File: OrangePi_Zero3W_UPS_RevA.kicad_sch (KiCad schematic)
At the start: 33 parts, among them J1 ORANGE_PI_ZERO_3W_HEADER, J2 BATTERY_1S_PROTECTED_NTC, J3 USB_C_POWER_INPUT, Q1 STL9P3LLH6, SW1 POWER / QON, U1 MAX17048G_T10, U2 BQ25895RTWR, U3 STUSB4500LQTR

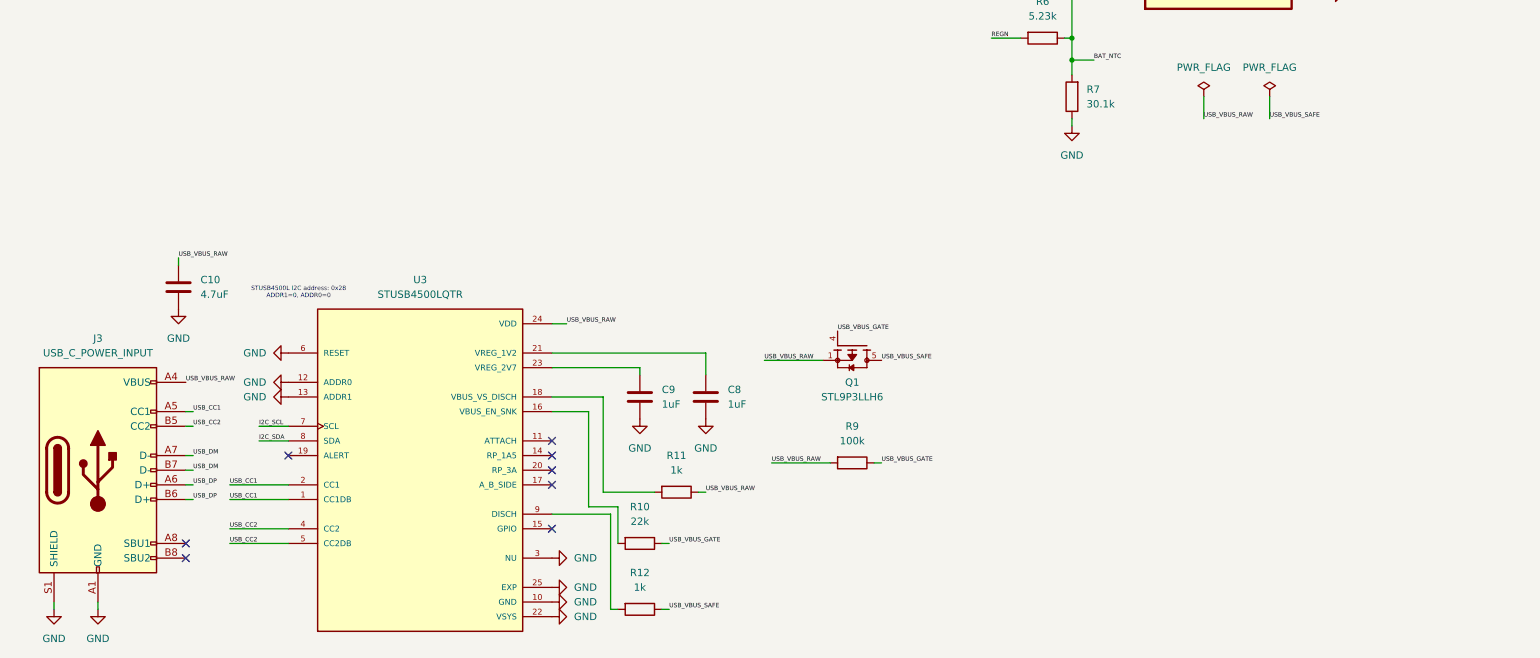
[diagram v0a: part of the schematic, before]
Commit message: Phase 5B.2D: add USB-C ESD and VBUS surge protection
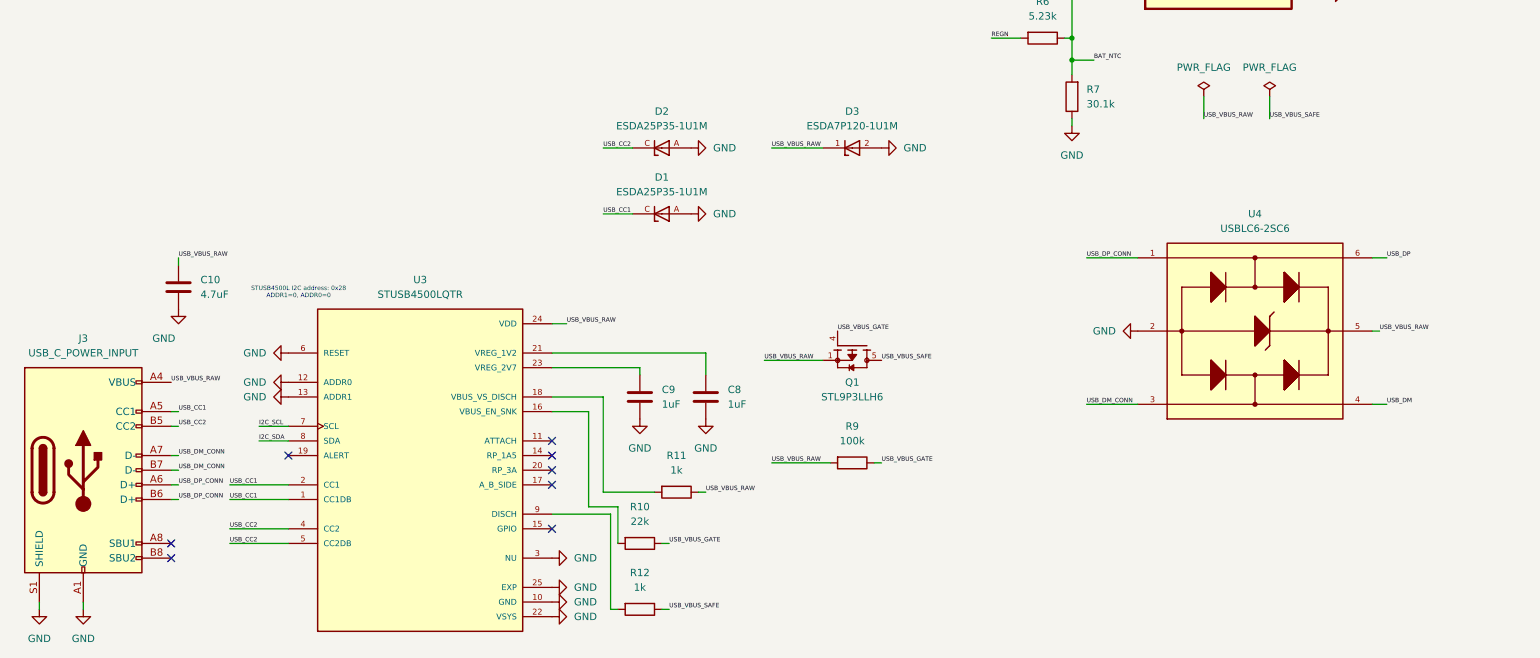
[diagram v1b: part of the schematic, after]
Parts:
- added D1, D2: ESDA25P35-1U1M, ESDA25P35-1U1M:TVS_ESDA25P35-1U1M, symbol ESDA25P35-1U1M:ESDA25P35-1U1M
- added D3: ESDA7P120-1U1M, ESDA7P120-1U1M:TVS_ESDA7P120-1U1M, symbol ESDA7P120-1U1M:ESDA7P120-1U1M
- added U4: USBLC6-2SC6, USBLC6-2SC6:SOT95P280X145-6N, symbol USBLC6-2SC6:USBLC6-2SC6
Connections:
- net GND: now also D1.A, D2.A, D3.2, U4.2
- net USB_CC1: now also D1.C
- net USB_CC2: now also D2.C
- net USB_DM: now also U4.4; no longer J3.A7 (D-), J3.B7 (D-)
- net USB_DP: now also U4.6; no longer J3.A6 (D+), J3.B6 (D+)
- net USB_VBUS_RAW: now also D3.1, U4.5
- new net USB_DM_CONN: J3.A7 (D-), J3.B7 (D-), U4.3
- new net USB_DP_CONN: J3.A6 (D+), J3.B6 (D+), U4.1
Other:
- moved on the sheet: J3

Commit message: Phase 5B.3: audit charger and USB-C input schematic
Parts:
- D3: Function SB 5V VBUS TVS -> USB 5V VBUS TVS
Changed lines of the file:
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@@
 			)
 		)
-		(property "Function" "SB 5V VBUS TVS"
+		(property "Function" "USB 5V VBUS TVS"
 			(at 157.48 105.41 0)
 			(effects

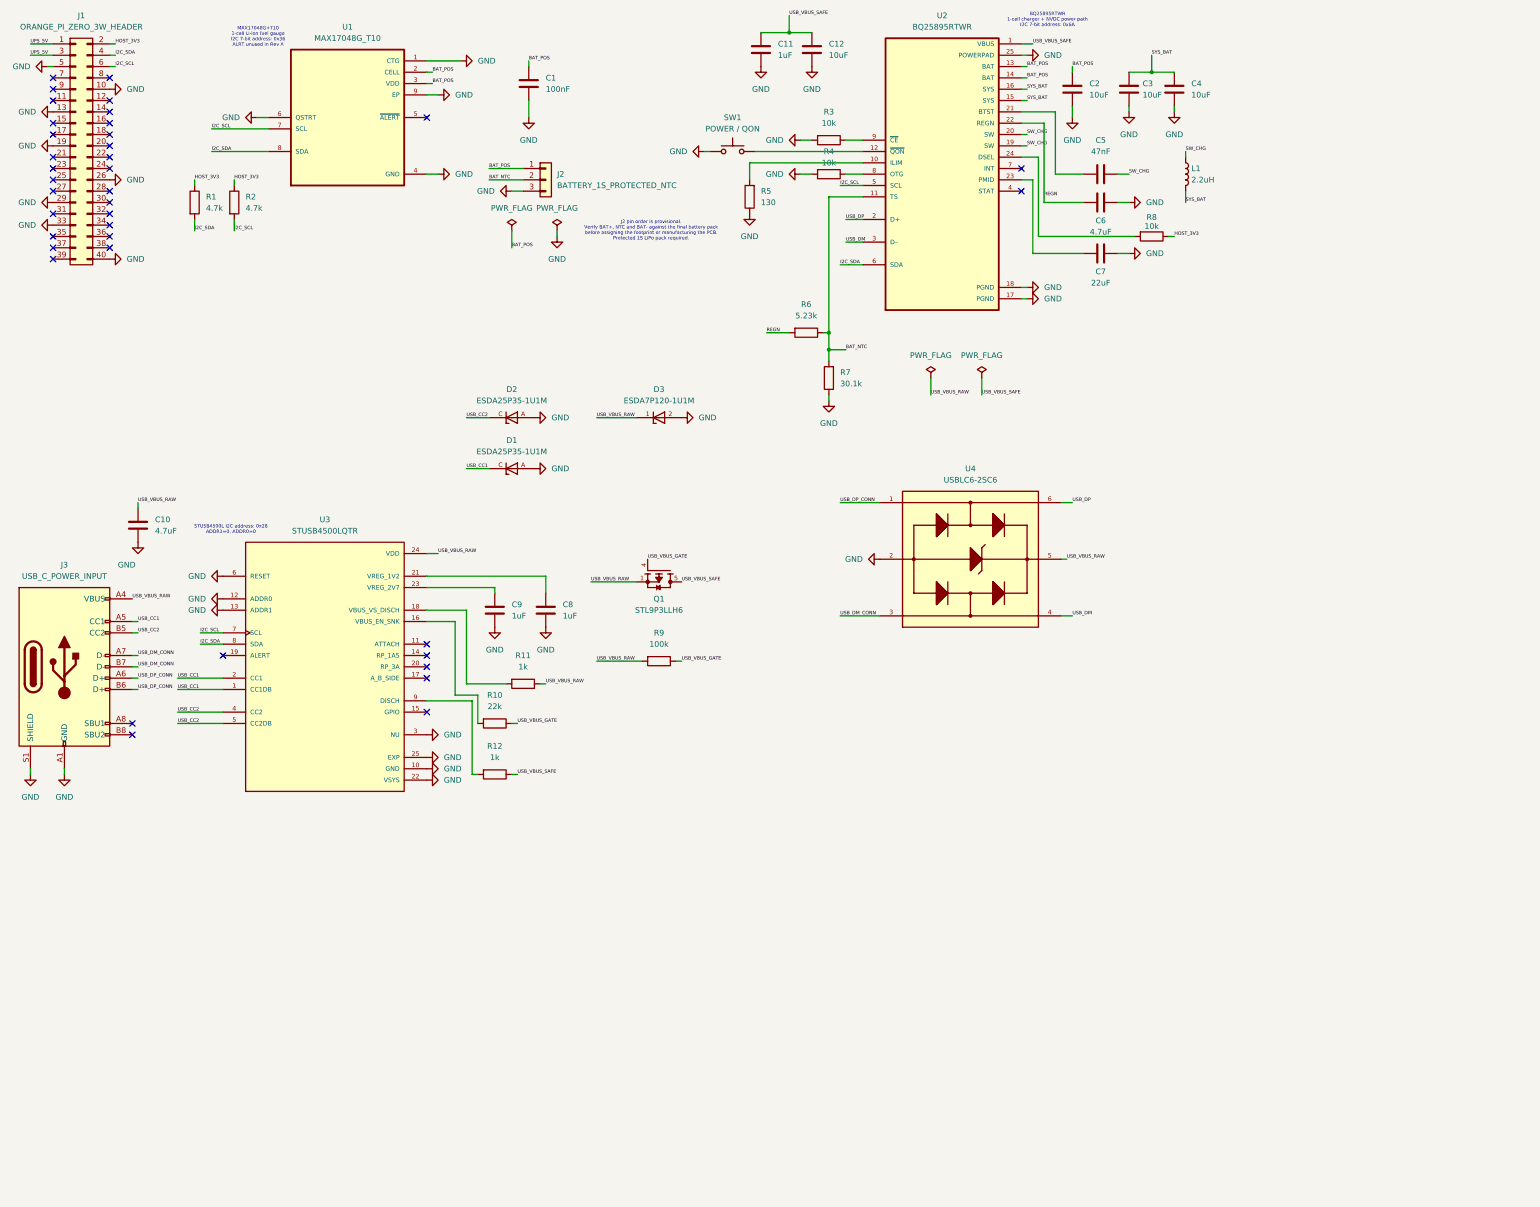
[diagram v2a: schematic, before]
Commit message: Phase 5C.1: import and validate TPS61088 boost converter
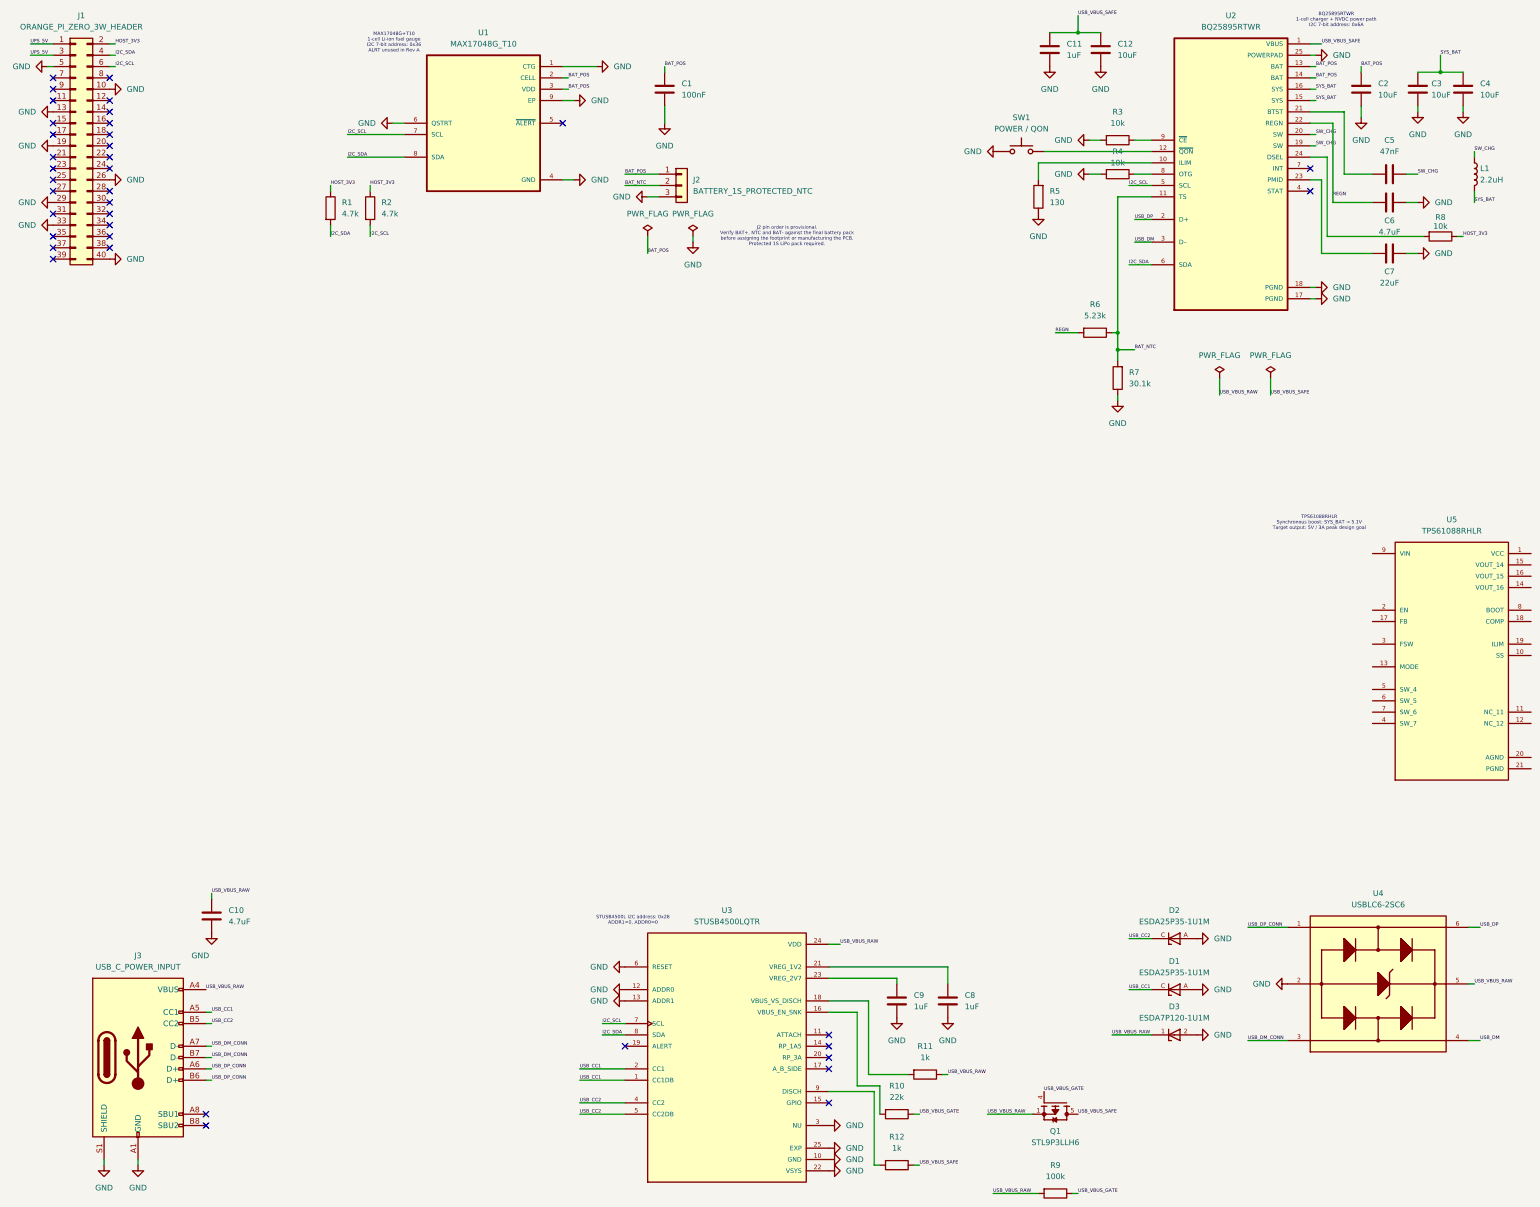
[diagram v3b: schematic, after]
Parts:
- added U5: TPS61088RHLR, TPS61088RHLR:IC_TPS61088RHLR, symbol TPS61088RHLR:TPS61088RHLR
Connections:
- new net PGND: U5.21 (PGND), U5.22 (PGND), U5.23 (PGND), U5.24 (PGND), U5.25 (PGND), U5.26 (PGND), U5.27 (PGND), U5.28 (PGND), U5.29 (PGND)
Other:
- note added: "TPS61088RHLR Synchronous boost: SYS_BAT → 5.1V Target output: 5V / 3A peak design goal"
- moved on the sheet: C1, C10, C11, C12, C2, C3, C4, C5, C6, C7, C8, C9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

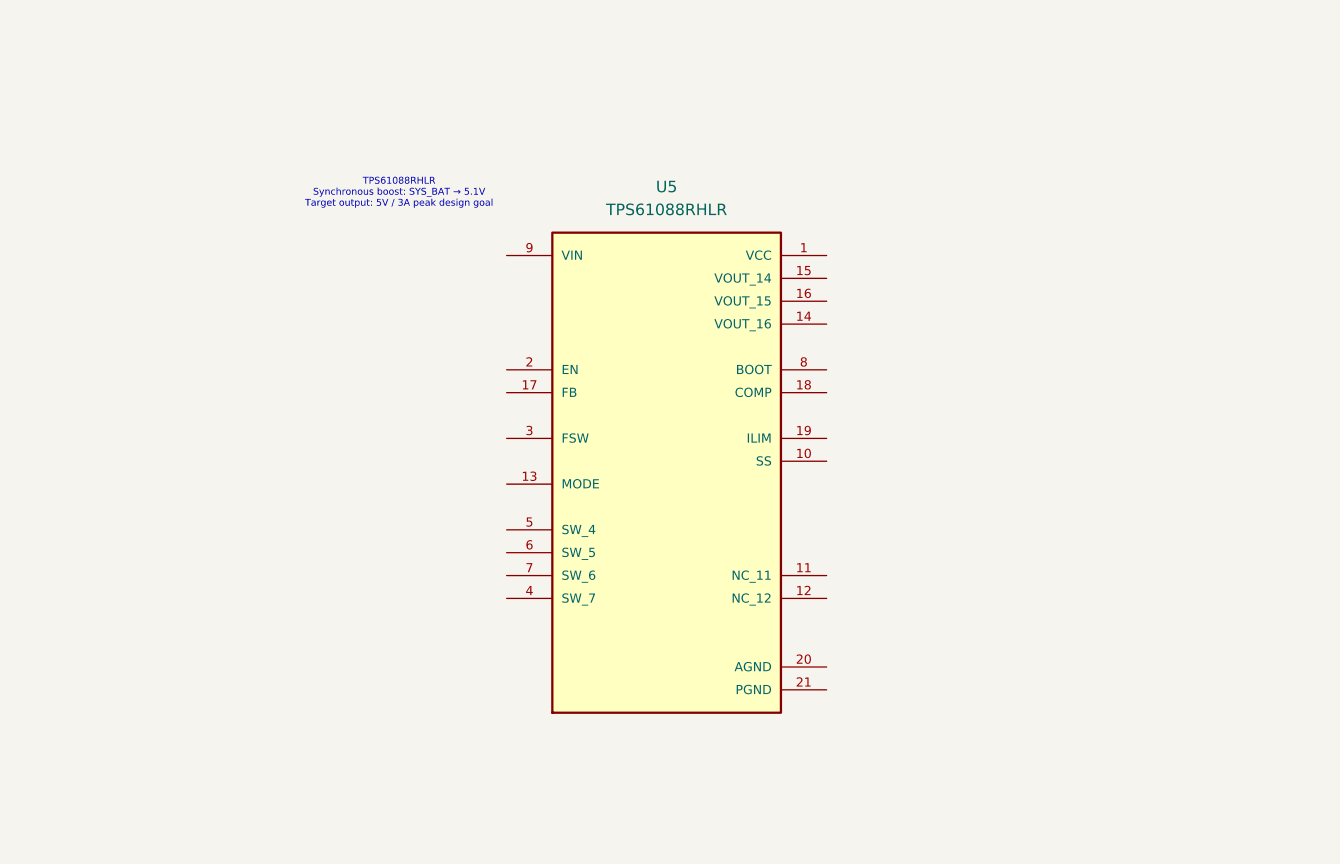
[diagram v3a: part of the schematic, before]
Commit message: Phase 5C.2A: add TPS61088 input supply and control configuration
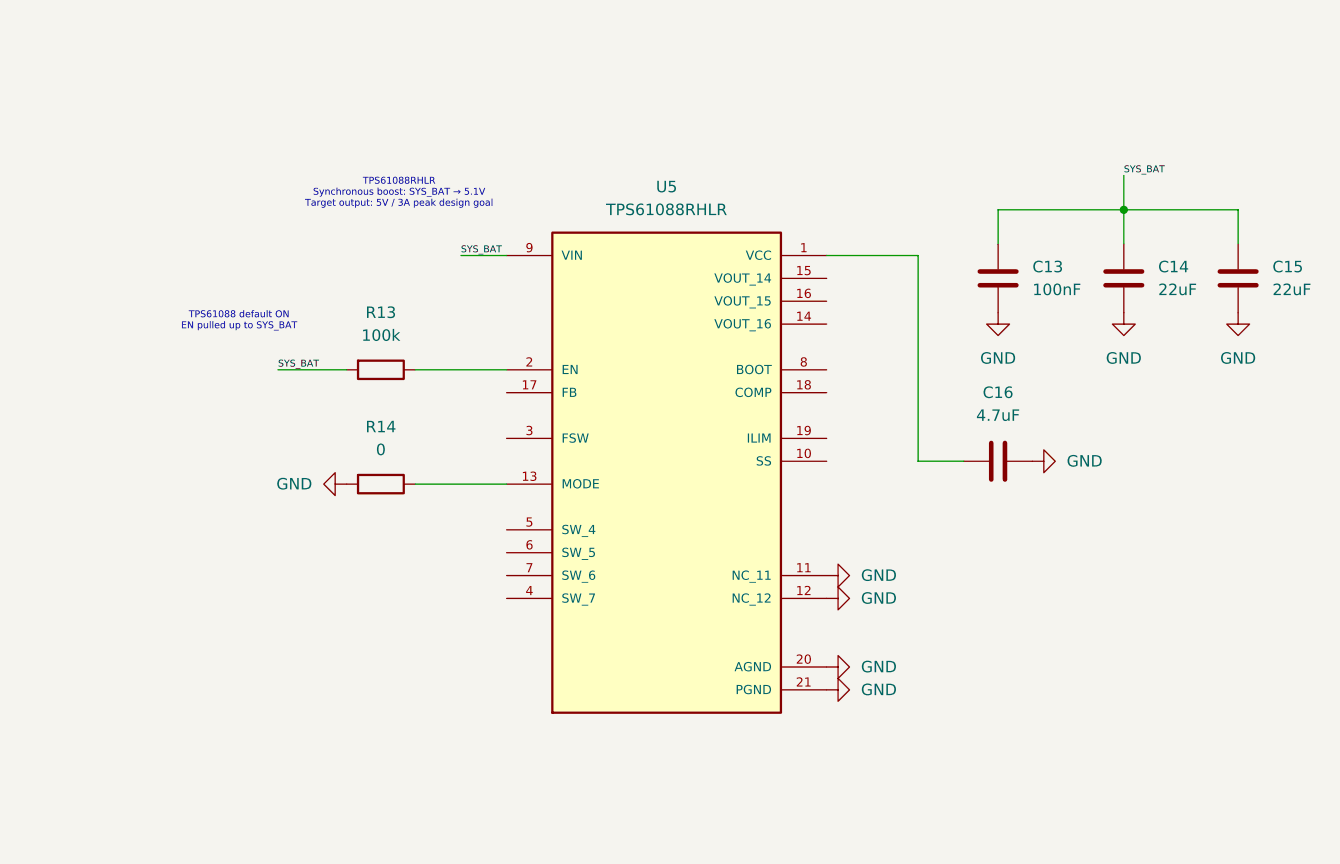
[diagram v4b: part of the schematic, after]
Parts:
- added C13: 100nF, Capacitor_SMD:C_0603_1608Metric, symbol Device:C
- added C14, C15: 22uF, Capacitor_SMD:C_1206_3216Metric, symbol Device:C
- added C16: 4.7uF, Capacitor_SMD:C_0603_1608Metric, symbol Device:C
- added R13: 100k, Resistor_SMD:R_0603_1608Metric, symbol Device:R
- added R14: 0, Resistor_SMD:R_0603_1608Metric, symbol Device:R
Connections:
- net PGND is gone; now on net GND: U5.21 (PGND), U5.22 (PGND), U5.23 (PGND), U5.24 (PGND), U5.25 (PGND), U5.26 (PGND), U5.27 (PGND), U5.28 (PGND), U5.29 (PGND)
- net GND: now also U5.11 (NC_11), U5.12 (NC_12), U5.20 (AGND), C13.2, C14.2, C15.2, C16.2, R14.2
- net SYS_BAT: now also U5.9 (VIN), C13.1, C14.1, C15.1, R13.2
- net at U5.1 (VCC): now also C16.1
- net at U5.13 (MODE): now also R14.1
- net at U5.2 (EN): now also R13.1
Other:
- note added: "TPS61088 default ON EN pulled up to SYS_BAT"
